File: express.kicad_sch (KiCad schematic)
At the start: 46 parts, among them J101 Cortex_Debug, J102 JAE_DX07S016JA3, SW101 SW_Push, SW102 SW_Push, U101 TPS78433QWDRBRQ1, U103 ATSAMD51J, Y102 32k768

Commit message: Fix LED location
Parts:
- U101: value TPS78433QWDRBRQ1 -> TPS78433QWDRBRQ1
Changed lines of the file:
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@@
 		(at 227.33 175.26 0)
 		(unit 1)
-		(exclude_from_sim no)
+		(exclude_from_sim yes)
 		(in_bom no)
 		(on_board yes)
@@
 			)
 		)
-		(property "Value" "TPS78433QWDRBRQ1 "
+		(property "Value" "TPS78433QWDRBRQ1"
 			(at 190.5 29.21 0)
 			(effects
@@
 		(at 248.92 162.56 0)
 		(unit 1)
-		(exclude_from_sim no)
+		(exclude_from_sim yes)
 		(in_bom no)
 		(on_board yes)
@@
 		(at 226.06 159.385 0)
 		(unit 1)
-		(exclude_from_sim no)
+		(exclude_from_sim yes)
 		(in_bom no)
 		(on_board yes)
@@
 		(at 172.72 160.02 0)
 		(unit 1)
-		(exclude_from_sim no)
+		(exclude_from_sim yes)
 		(in_bom yes)
 		(on_board yes)
@@
 		(at 172.72 182.88 0)
 		(unit 1)
-		(exclude_from_sim no)
+		(exclude_from_sim yes)
 		(in_bom yes)
 		(on_board yes)
@@
 		(at 132.08 96.52 0)
 		(unit 1)
-		(exclude_from_sim no)
+		(exclude_from_sim yes)
 		(in_bom no)
 		(on_board yes)
@@
 		(at 248.92 175.26 0)
 		(unit 1)
-		(exclude_from_sim no)
+		(exclude_from_sim yes)
 		(in_bom no)
 		(on_board yes)
@@
 		(at 172.72 167.64 0)
 		(unit 1)
-		(exclude_from_sim no)
+		(exclude_from_sim yes)
 		(in_bom yes)
 		(on_board yes)
@@
 		(at 205.74 177.8 0)
 		(unit 1)
-		(exclude_from_sim no)
+		(exclude_from_sim yes)
 		(in_bom no)
 		(on_board yes)
@@
 		(at 172.72 175.26 0)
 		(unit 1)
-		(exclude_from_sim no)
+		(exclude_from_sim yes)
 		(in_bom yes)
 		(on_board yes)
@@
 		(at 275.59 149.86 0)
 		(unit 1)
-		(exclude_from_sim no)
+		(exclude_from_sim yes)
 		(in_bom no)
 		(on_board yes)
@@
 		(at 248.92 149.86 0)
 		(unit 1)
-		(exclude_from_sim no)
+		(exclude_from_sim yes)
 		(in_bom no)
 		(on_board yes)
@@
 		(at 172.72 152.4 0)
 		(unit 1)
-		(exclude_from_sim no)
+		(exclude_from_sim yes)
 		(in_bom yes)
 		(on_board yes)
@@
 		(at 275.59 162.56 0)
 		(unit 1)
-		(exclude_from_sim no)
+		(exclude_from_sim yes)
 		(in_bom no)
 		(on_board yes)
@@
 		(at 185.42 101.6 0)
 		(unit 1)
-		(exclude_from_sim no)
+		(exclude_from_sim yes)
 		(in_bom yes)
 		(on_board yes)
@@
 		(at 275.59 175.26 0)
 		(unit 1)
-		(exclude_from_sim no)
+		(exclude_from_sim yes)
 		(in_bom no)
 		(on_board yes)
@@
 		(at 204.47 168.91 0)
 		(unit 1)
-		(exclude_from_sim no)
+		(exclude_from_sim yes)
 		(in_bom no)
 		(on_board yes)
@@
 		(at 205.74 153.67 0)
 		(unit 1)
-		(exclude_from_sim no)
+		(exclude_from_sim yes)
 		(in_bom no)
 		(on_board yes)

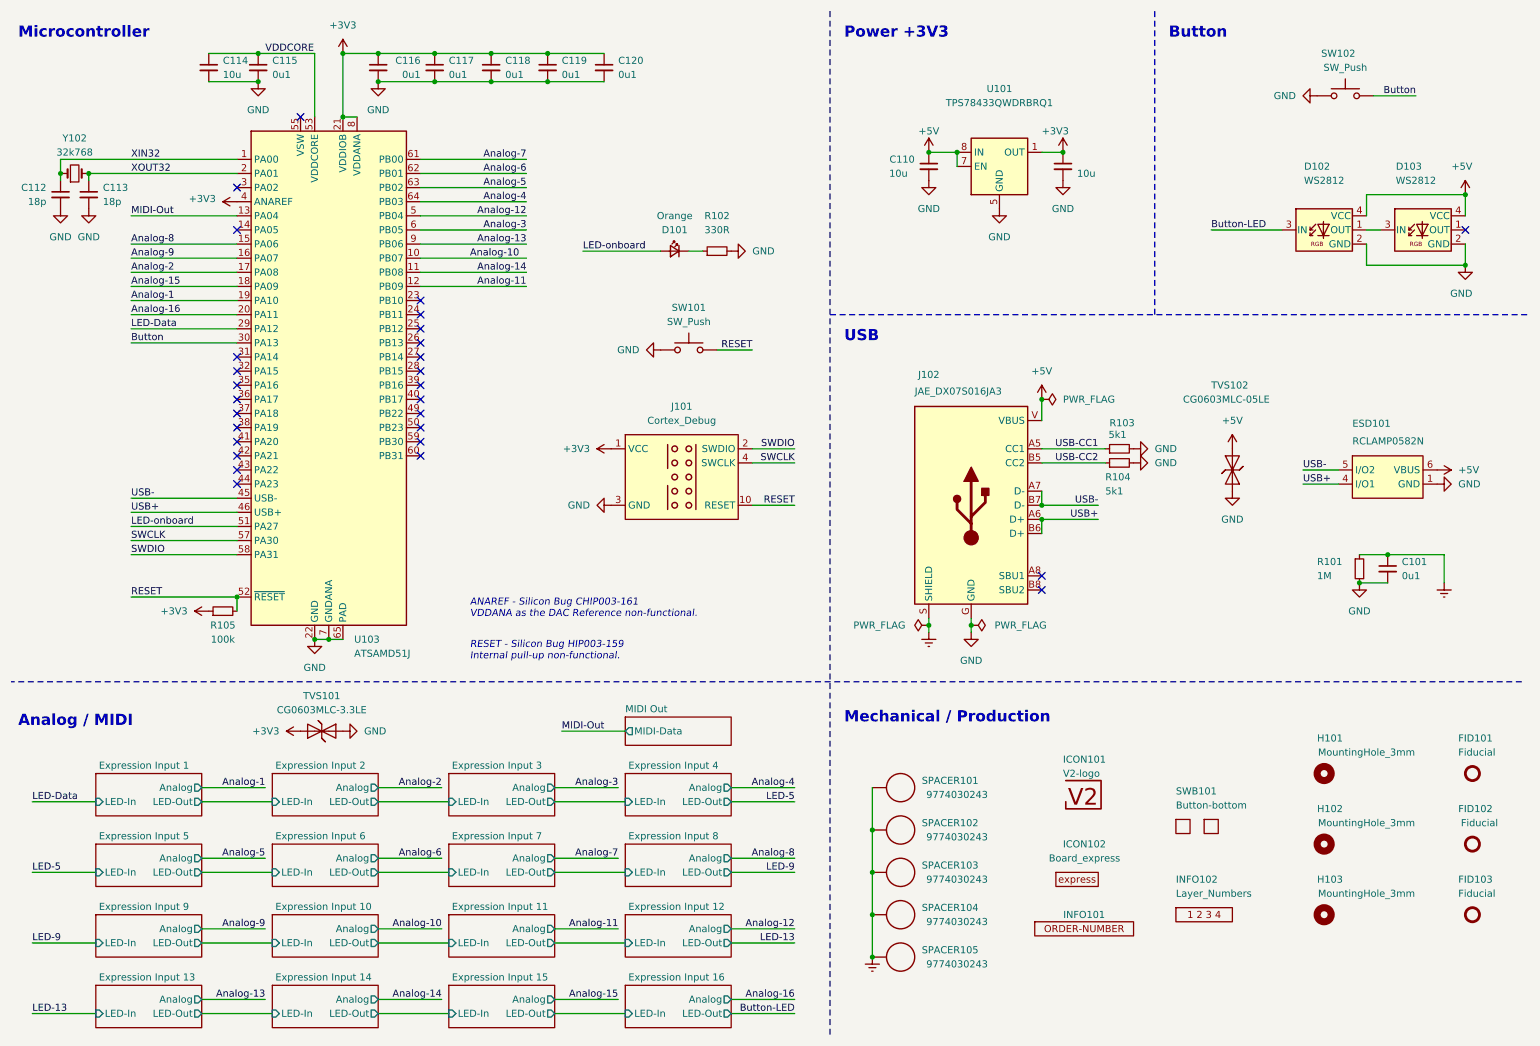
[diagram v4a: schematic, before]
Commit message: Convert to V2 Link
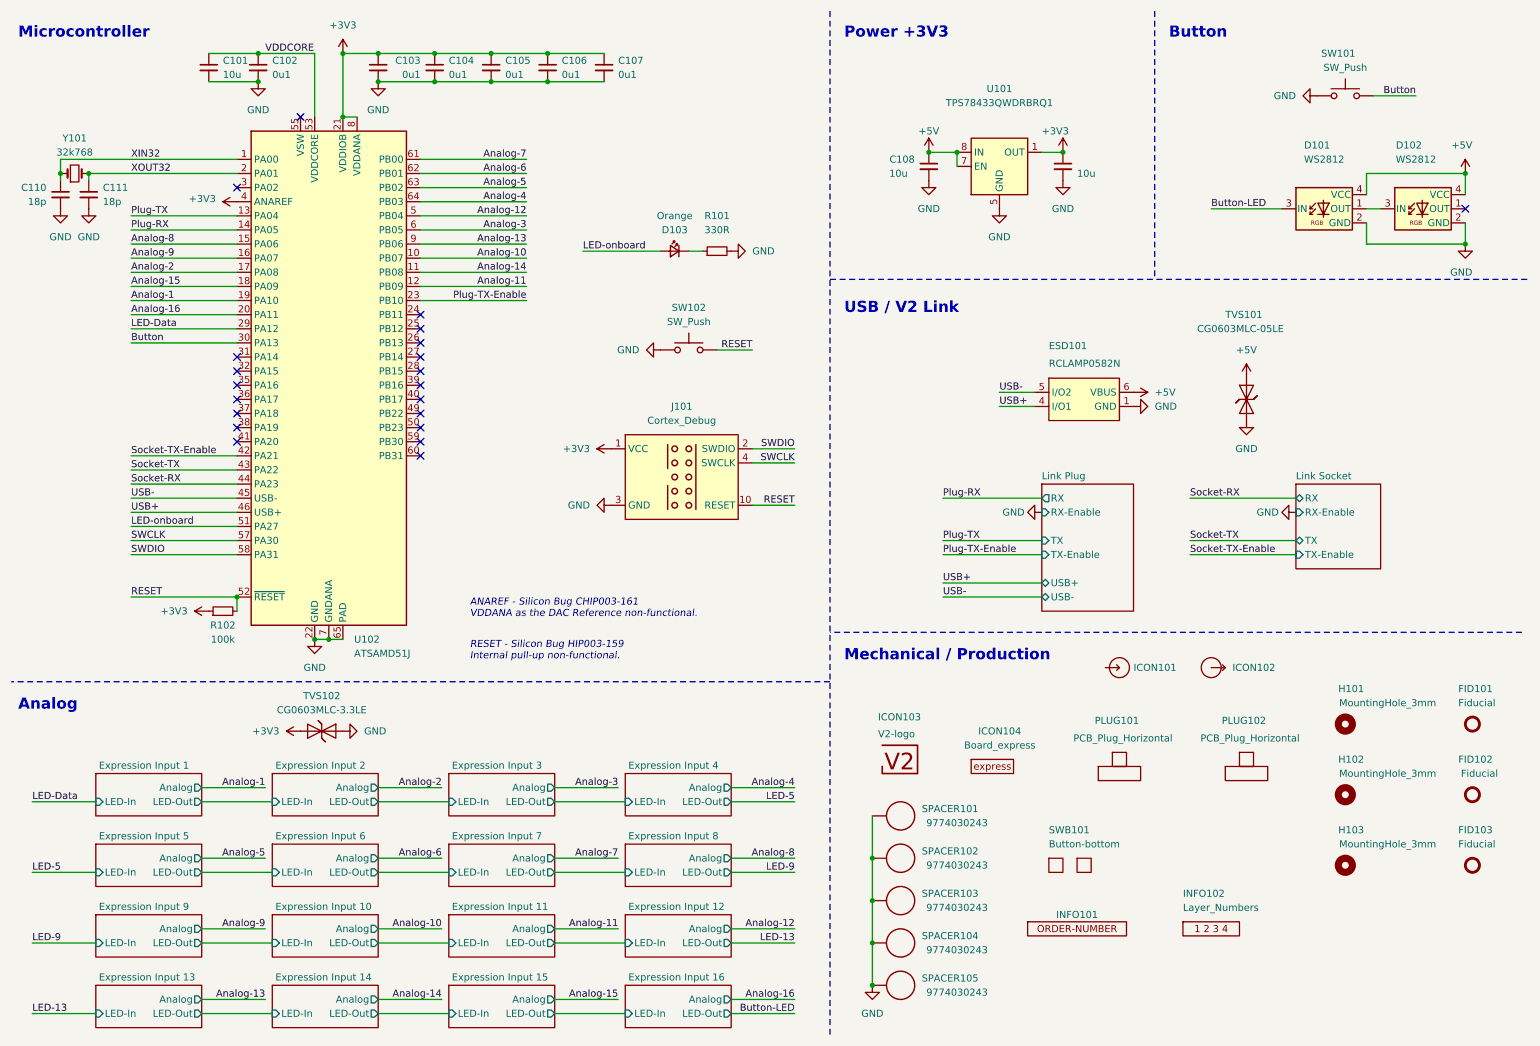
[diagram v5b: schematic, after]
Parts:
- removed C101: 0u1, Capacitor_SMD:C_0603_1608Metric, symbol Device:C_Small
- removed J102: JAE_DX07S016JA3, V2_Connector_USB:JAE_DX07S016JA3, symbol V2_Connector_USB:JAE_DX07S016JA3
- removed R101: 1M, Resistor_SMD:R_0603_1608Metric, symbol Device:R_Small
- removed R103, R104: 5k1, Resistor_SMD:R_0603_1608Metric, symbol Device:R_Small
- added ICON101: Arrow_In, V2_Artwork:Arrow_In, symbol V2_Artwork:Arrow_In
- added ICON102: Arrow_Out, V2_Artwork:Arrow_Out, symbol V2_Artwork:Arrow_Out
- added PLUG101, PLUG102: PCB_Plug_Horizontal, V2_PCB_Devices:PCB_Plug_Horizontal, symbol V2_PCB_Devices:PCB_Plug_Horizontal
- renumbered C114 to C101, C115 to C102, C116 to C103, C117 to C104, C118 to C105, C119 to C106, C120 to C107, C110 to C108, C121 to C109, C112 to C110, C113 to C111, D102 to D101, D103 to D102, D101 to D103, ICON101 to ICON103, ICON102 to ICON104, R102 to R101, R105 to R102, SW102 to SW101, SW101 to SW102, TVS102 to TVS101, TVS101 to TVS102, U103 to U102, Y102 to Y101
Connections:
- net Earth is gone; now on net GND: SPACER101.1, SPACER102.1, SPACER103.1, SPACER104.1, SPACER105.1
- net Plug-RX: now reaches U102.14 (PA05)
- net Plug-TX-Enable: now reaches U102.23 (PB10)
- net Socket-TX-Enable: now reaches U102.42 (PA21)
- net Socket-TX: now reaches U102.43 (PA22)
- net Socket-RX: now reaches U102.44 (PA23)
- net MIDI-Out renamed Plug-TX
- no-connect marks 28 -> 21
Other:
- removed sheet MIDI Out
- added sheet Link Plug (LinkPlug.kicad_sch)
- added sheet Link Socket (LinkSocket.kicad_sch)
- note added: "Analog"
- note added: "USB / V2 Link"
- note removed: "Analog / MIDI"
- note removed: "USB"
- moved on the sheet: D101, D102, ESD101, FID101, FID102, FID103, H101, H102, H103, ICON103, ICON104, INFO101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

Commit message: Update tranceiver
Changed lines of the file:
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@@
 	(title_block
 		(title "V2 express")
-		(date "2025-09-19")
-		(rev "2")
+		(date "2025-10-26")
+		(rev "3")
 		(company "Versio Duo")
 		(comment 1 "Expression Controller")
@@
 		(at 228.6 130.81 0)
 		(unit 1)
-		(exclude_from_sim yes)
+		(exclude_from_sim no)
 		(in_bom no)
 		(on_board yes)
@@
 			)
 		)
+		(property "Sim.Enable" "0"
+			(at 228.6 130.81 0)
+			(effects
+				(font
+					(size 1.27 1.27)
+				)
+				(hide yes)
+			)
+		)
 		(instances
 			(project "express"
@@
 		(at 228.6 177.8 0)
 		(unit 1)
-		(exclude_from_sim yes)
+		(exclude_from_sim no)
 		(in_bom no)
 		(on_board yes)
@@
 			)
 		)
+		(property "Sim.Enable" "0"
+			(at 228.6 177.8 0)
+			(effects
+				(font
+					(size 1.27 1.27)
+				)
+				(hide yes)
+			)
+		)
 		(instances
 			(project "express"
@@
 		(at 252.73 153.67 0)
 		(unit 1)
-		(exclude_from_sim yes)
+		(exclude_from_sim no)
 		(in_bom no)
 		(on_board yes)
@@
 			)
 		)
+		(property "Sim.Enable" "0"
+			(at 252.73 153.67 0)
+			(effects
+				(font
+					(size 1.27 1.27)
+				)
+				(hide yes)
+			)
+		)
 		(instances
 			(project "express"
@@
 		(at 203.2 166.37 0)
 		(unit 1)
-		(exclude_from_sim yes)
+		(exclude_from_sim no)
 		(in_bom no)
 		(on_board yes)
@@
 			)
 		)
+		(property "Sim.Enable" "0"
+			(at 203.2 166.37 0)
+			(effects
+				(font
+					(size 1.27 1.27)
+				)
+				(hide yes)
+			)
+		)
 		(instances
 			(project "express"
@@
 		(at 172.72 165.1 0)
 		(unit 1)
-		(exclude_from_sim yes)
+		(exclude_from_sim no)
 		(in_bom yes)
 		(on_board yes)
@@
 			)
 		)
+		(property "Sim.Enable" "0"
+			(at 172.72 165.1 0)
+			(effects
+				(font
+					(size 1.27 1.27)
+				)
+				(hide yes)
+			)
+		)
 		(pin "1"
 		)
@@
 		(at 172.72 187.96 0)
 		(unit 1)
-		(exclude_from_sim yes)
+		(exclude_from_sim no)
 		(in_bom yes)
 		(on_board yes)
@@
 			)
 		)
+		(property "Sim.Enable" "0"
+			(at 172.72 187.96 0)
+			(effects
+				(font
+					(size 1.27 1.27)
+				)
+				(hide yes)
+			)
+		)
 		(pin "1"
 		)
@@
 		(at 132.08 96.52 0)
 		(unit 1)
-		(exclude_from_sim yes)
+		(exclude_from_sim no)
 		(in_bom no)
 		(on_board yes)
@@
 			)
 		)
+		(property "Sim.Enable" "0"
+			(at 132.08 96.52 0)
+			(effects
+				(font
+					(size 1.27 1.27)
+				)
+				(hide yes)
+			)
+		)
 		(pin "1"
 		)
@@
 		(at 252.73 166.37 0)
 		(unit 1)
-		(exclude_from_sim yes)
+		(exclude_from_sim no)
 		(in_bom no)
 		(on_board yes)
@@
 			)
 		)
+		(property "Sim.Enable" "0"
+			(at 252.73 166.37 0)
+			(effects
+				(font
+					(size 1.27 1.27)
+				)
+				(hide yes)
+			)
+		)
 		(instances
 			(project "express"
@@
 		(at 172.72 172.72 0)
 		(unit 1)
-		(exclude_from_sim yes)
+		(exclude_from_sim no)
 		(in_bom yes)
 		(on_board yes)
@@
 			)
 		)
+		(property "Sim.Enable" "0"
+			(at 172.72 172.72 0)
+			(effects
+				(font
+					(size 1.27 1.27)
+				)
+				(hide yes)
+			)
+		)
 		(pin "1"
 		)
@@
 		(at 204.47 177.8 0)
 		(unit 1)
-		(exclude_from_sim yes)
+		(exclude_from_sim no)
 		(in_bom no)
 		(on_board yes)
@@
 			)
 		)
+		(property "Sim.Enable" "0"
+			(at 204.47 177.8 0)
+			(effects
+				(font
+					(size 1.27 1.27)
+				)
+				(hide yes)
+			)
+		)
 		(instances
 			(project "express"
@@
 		(at 212.09 148.59 0)
 		(unit 1)
-		(exclude_from_sim yes)
+		(exclude_from_sim no)
 		(in_bom no)
 		(on_board yes)
@@
 			)
 		)
+		(property "Sim.Enable" "0"
+			(at 212.09 148.59 0)
+			(effects
+				(font
+					(size 1.27 1.27)
+				)
+				(hide yes)
+			)
+		)
 		(instances
 			(project "express"
@@
 		(at 172.72 180.34 0)
 		(unit 1)
-		(exclude_from_sim yes)
+		(exclude_from_sim no)
 		(in_bom yes)
 		(on_board yes)
@@
 			)
 		)
+		(property "Sim.Enable" "0"
+			(at 172.72 180.34 0)
+			(effects
+				(font
+					(size 1.27 1.27)
+				)
+				(hide yes)
+			)
+		)
 		(pin "1"
 		)
@@
 		(at 275.59 140.97 0)
 		(unit 1)
-		(exclude_from_sim yes)
+		(exclude_from_sim no)
 		(in_bom no)
 		(on_board yes)
@@
 			)
 		)
+		(property "Sim.Enable" "0"
+			(at 275.59 140.97 0)
+			(effects
+				(font
+					(size 1.27 1.27)
+				)
+				(hide yes)
+			)
+		)
 		(instances
 			(project "express"
@@
 		(at 252.73 140.97 0)
 		(unit 1)
-		(exclude_from_sim yes)
+		(exclude_from_sim no)
 		(in_bom no)
 		(on_board yes)
@@
 			)
 		)
+		(property "Sim.Enable" "0"
+			(at 252.73 140.97 0)
+			(effects
+				(font
+					(size 1.27 1.27)
+				)
+				(hide yes)
+			)
+		)
 		(instances
 			(project "express"
@@
 		(at 172.72 157.48 0)
 		(unit 1)
-		(exclude_from_sim yes)
+		(exclude_from_sim no)
 		(in_bom yes)
 		(on_board yes)
@@
 			)
 		)
+		(property "Sim.Enable" "0"
+			(at 172.72 157.48 0)
+			(effects
+				(font
+					(size 1.27 1.27)
+				)
+				(hide yes)
+			)
+		)
 		(pin "1"
 		)
@@
 		(at 275.59 153.67 0)
 		(unit 1)
-		(exclude_from_sim yes)
+		(exclude_from_sim no)
 		(in_bom no)
 		(on_board yes)
@@
 			)
 		)
+		(property "Sim.Enable" "0"
+			(at 275.59 153.67 0)
+			(effects
+				(font
+					(size 1.27 1.27)
+				)
+				(hide yes)
+			)
+		)
 		(instances
 			(project "express"
@@
 		(at 212.09 130.81 0)
 		(unit 1)
-		(exclude_from_sim yes)
+		(exclude_from_sim no)
 		(in_bom no)
 		(on_board yes)
@@
 			)
 		)
+		(property "Sim.Enable" "0"
+			(at 212.09 130.81 0)
+			(effects
+				(font
+					(size 1.27 1.27)
+				)
+				(hide yes)
+			)
+		)
 		(instances
 			(project "express"
@@
 		(at 275.59 166.37 0)
 		(unit 1)
-		(exclude_from_sim yes)
+		(exclude_from_sim no)
 		(in_bom no)
 		(on_board yes)
@@
 			)
 		)
+		(property "Sim.Enable" "0"
+			(at 275.59 166.37 0)
+			(effects
+				(font
+					(size 1.27 1.27)
+				)
+				(hide yes)
+			)
+		)
 		(instances
 			(project "express"
@@
 		(at 189.23 148.59 0)
 		(unit 1)
-		(exclude_from_sim yes)
+		(exclude_from_sim no)
 		(in_bom no)
 		(on_board yes)
@@
 			)
 		)
+		(property "Sim.Enable" "0"
+			(at 189.23 148.59 0)
+			(effects
+				(font
+					(size 1.27 1.27)
+				)
+				(hide yes)
+			)
+		)
 		(instances
 			(project "express"
@@
 		(at 172.72 147.32 0)
 		(unit 1)
-		(exclude_from_sim yes)
+		(exclude_from_sim no)
 		(in_bom no)
 		(on_board yes)
@@
 			)
 		)
+		(property "Sim.Enable" "0"
+			(at 172.72 147.32 0)
+			(effects
+				(font
+					(size 1.27 1.27)
+				)
+				(hide yes)
+			)
+		)
 		(instances
 			(project "express"
@@
 		(at 234.95 148.59 0)
 		(unit 1)
-		(exclude_from_sim yes)
+		(exclude_from_sim no)
 		(in_bom no)
 		(on_board yes)
@@
 			(at 234.95 148.59 0)
 			(effects
+				(font
+					(size 1.27 1.27)
+				)
+				(hide yes)
+			)
+		)
+		(property "Sim.Enable" "0"
+			(at 234.95 148.59 0)
+			(effects

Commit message: Colours
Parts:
- removed C102: 0u1, Capacitor_SMD:C_0603_1608Metric, symbol Device:C_Small
- H103: renamed from SPACER101; value 9774030243 -> MountingHole_2mm; footprint V2_Spacer_Wurth:9774030243 -> V2_Mechanical:MountingHole_2mm; symbol V2_Spacer_Wurth:9774030243 -> V2_Mechanical:MountingHole_2mm; now left out of the parts list
- H104: renamed from SPACER102; value 9774030243 -> MountingHole_2mm; footprint V2_Spacer_Wurth:9774030243 -> V2_Mechanical:MountingHole_2mm; symbol V2_Spacer_Wurth:9774030243 -> V2_Mechanical:MountingHole_2mm; now left out of the parts list
- H106: renamed from SPACER103; value 9774030243 -> MountingHole_2mm; footprint V2_Spacer_Wurth:9774030243 -> V2_Mechanical:MountingHole_2mm; symbol V2_Spacer_Wurth:9774030243 -> V2_Mechanical:MountingHole_2mm; now left out of the parts list
- H107: renamed from SPACER104; value 9774030243 -> MountingHole_2mm; footprint V2_Spacer_Wurth:9774030243 -> V2_Mechanical:MountingHole_2mm; symbol V2_Spacer_Wurth:9774030243 -> V2_Mechanical:MountingHole_2mm; now left out of the parts list
- H108: renamed from SPACER105; value 9774030243 -> MountingHole_2mm; footprint V2_Spacer_Wurth:9774030243 -> V2_Mechanical:MountingHole_2mm; symbol V2_Spacer_Wurth:9774030243 -> V2_Mechanical:MountingHole_2mm; now left out of the parts list
- renumbered H103 to H105
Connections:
- net GND: no longer H103.1, H104.1, H106.1, H107.1, H108.1
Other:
- moved on the sheet: C101
